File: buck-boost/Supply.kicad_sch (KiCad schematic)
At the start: 29 parts, among them U16 LMR33630ADDA, U18 LMR62014XMF_NOPB

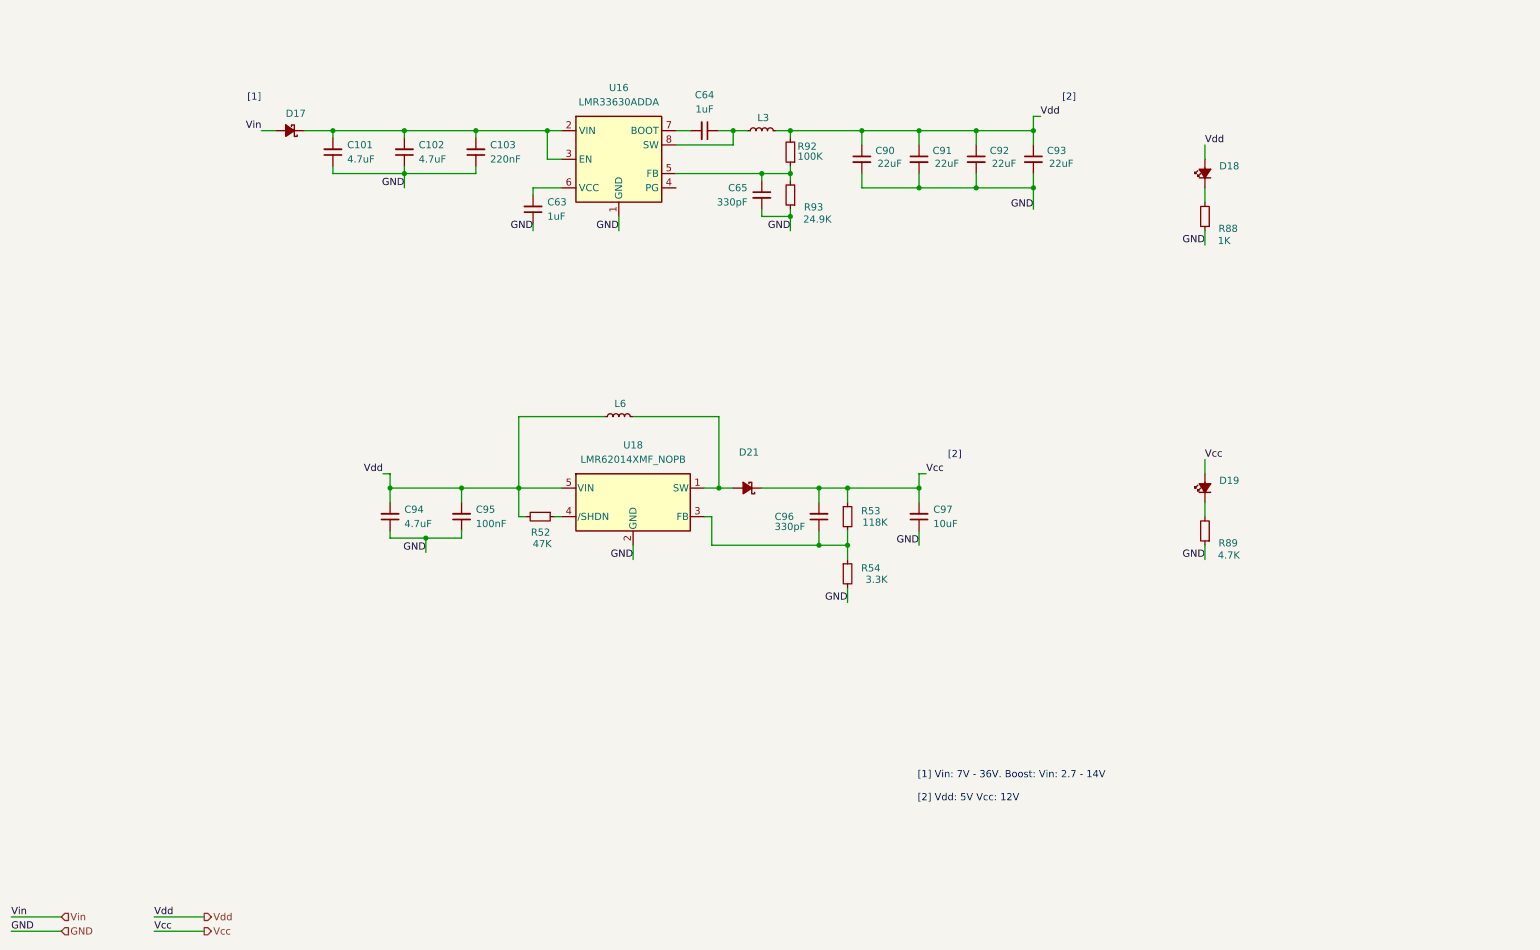
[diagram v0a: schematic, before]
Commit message: The changes indicated in the text document Review. 05.11.2024 were implemented. Missing footprints were added
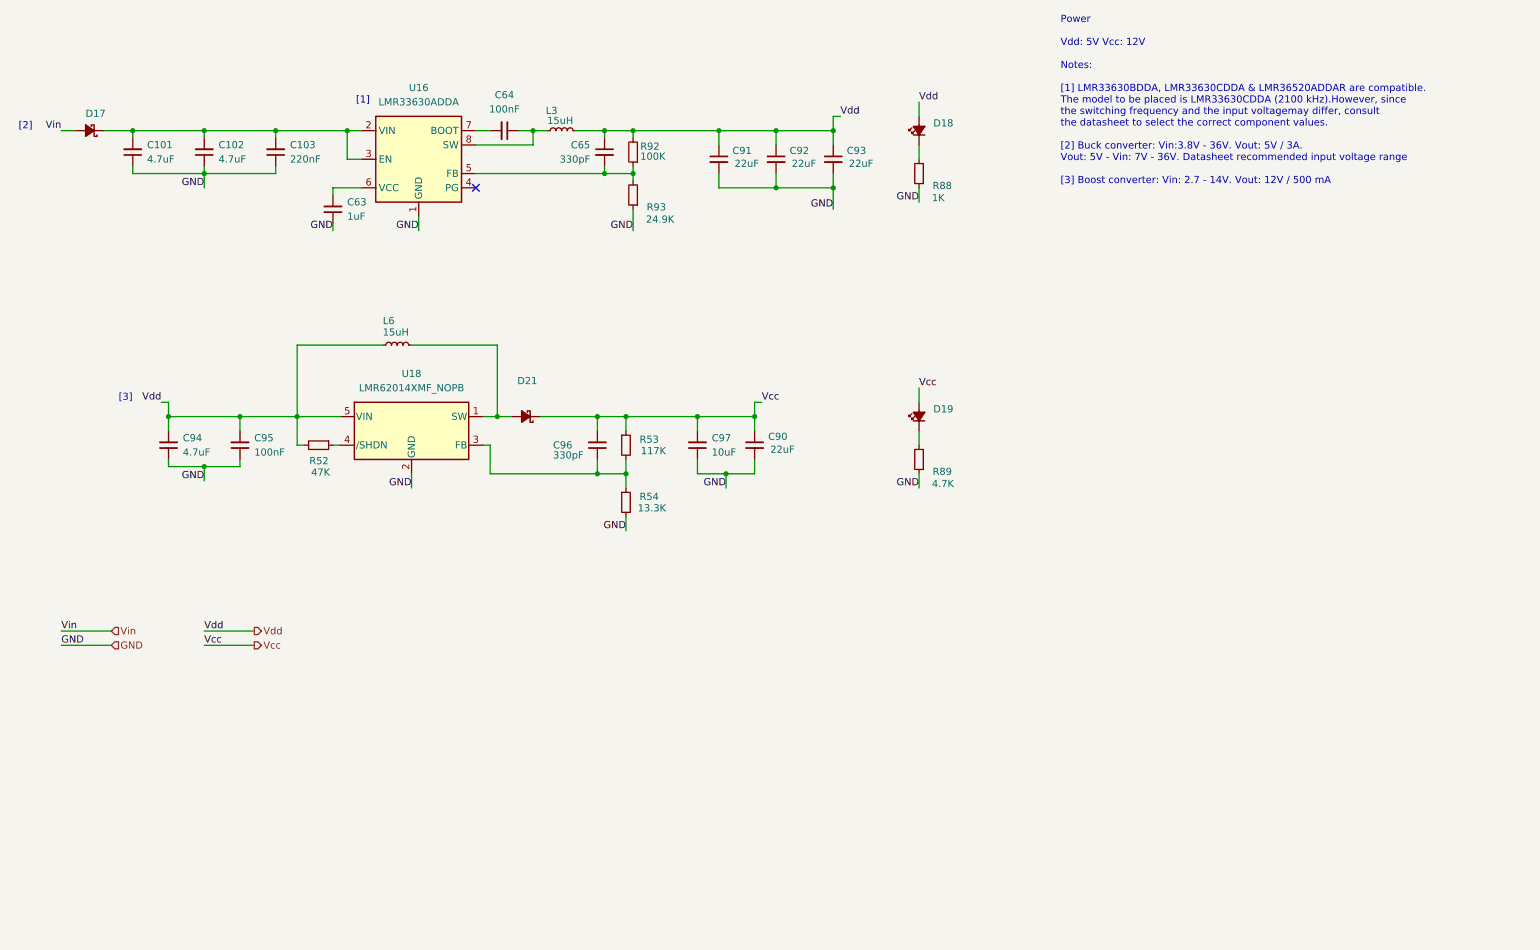
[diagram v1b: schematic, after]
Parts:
- C64: value 1uF -> 100nF
- L3, L6: value L_Small -> 15uH
- R53: value 118K -> 117K
- R54: value 3.3K -> 13.3K
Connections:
- net GND: no longer C65.2
- net Vcc: now also C90.1
- net Vdd: now also C65.1; no longer C90.1
- net at R92.1, R93.2, U16.5 (FB): now also C65.2; no longer C65.1
- no-connect marks 0 -> 1
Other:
- note added: "Power Vdd: 5V Vcc: 12V Notes: [1] LMR33630BDDA, LMR33630CDDA & LMR36520ADDAR are compatible. The model to be placed is LMR33630CDDA (2100 kHz).However, since the switching frequency and the input voltagemay differ, consult the datasheet to select the correct component values. [2] Buck converter: Vin:3.8V - 36V. Vout: 5V / 3A. Vout: 5V - Vin: 7V - 36V. Datasheet recommended input voltage range [3]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"
- note added: "[3]"
- note removed: "[1] Vin: 7V - 36V. Boost: Vin: 2.7 - 14V [2] Vdd: 5V Vcc: 12V"
- moved on the sheet: C101, C102, C103, C63, C64, C65, C90, C91, C92, C93, C94, C95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
